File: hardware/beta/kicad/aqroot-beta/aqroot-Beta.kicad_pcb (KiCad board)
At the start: 4 copper layers, 74 x 155 mm, 188 parts, among them J1 CH280QV10-CT_50P, J2 Molex_5025700893, J3 USB_C_Receptacle_USB2.0_16P, J4 JST-PH-2 BATTERY, J5 COMMUNITY_HEADER_2x13, J6 JST-PH-2 SPEAKER, Q1 AO3400A, SW1 BOOT, SW2 UP, SW3 DOWN, SW4 LEFT, SW5 RIGHT, SW6 A_SELECT, SW7 B_BACK, SW8 HOME, SW9 SW_SPDT, U1 ESP32-S3-WROOM-1, U10 USBLC6-2SC6, U11 BQ25185, U12 TPS63020, U13 TPS61023, U14 MAX17048, U15 TPS22918, U16 TCA9517ADGK, U17 TPS61169DCKR, U2 TCA9535PWR, U3 TCA9535PWR, U4 BMI270, U5 MAX98357A, U6 TSOP38238, U7 E07-400M10S, U8 E22-900M22S, U9 ST25R3916-AQET

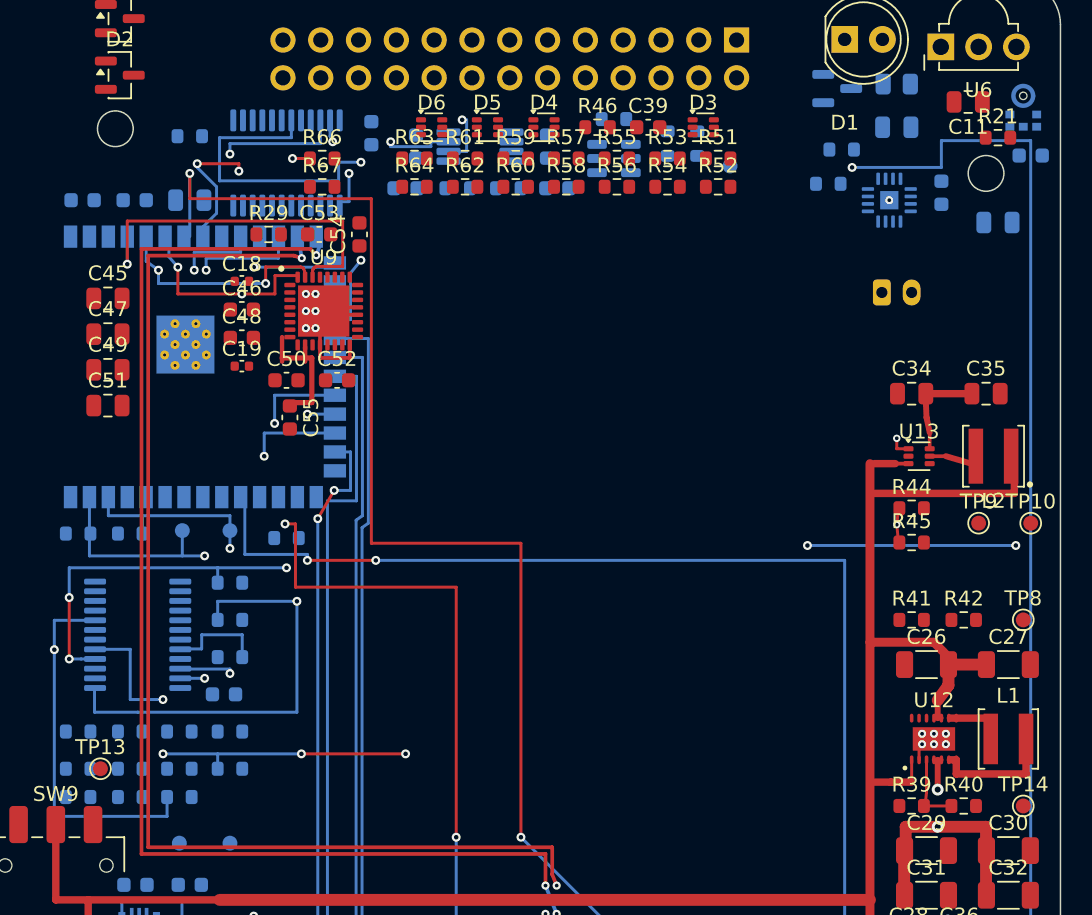
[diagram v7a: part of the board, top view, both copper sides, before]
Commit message: route +3V3 north backbone (Pass A: clusters F/C/B/A)
Builds the north +3V3 tree from the TPS63020 output island: 205.135 mm of
new copper in 57 tracks and 9 vias across B.Cu 38 / F.Cu 14 / In2 5. Board
ratsnest 405 -> 384, +3V3 ratsnest 69 -> 48, +3V3 islands 70 -> 49. DRC 0
electrical errors.

All 27 Pass-A pads now sit on ONE island with the U12 source: the six that
were already tied (U12.4, U12.5, C29.1, C30.1, C31.1, C32.1) plus the 21
routed here. Cluster F adds R39.1 and R41.1; cluster C adds U5.7, U5.8,
C9.1, C12.2, R24.2, C10.1, R21.1, C8.1, MK1.5, U15.1; cluster B adds
U16.1, C37.1, C40.1, C5.1, U3.24; cluster A adds C2.1, C3.1, R1.2, U1.2.

Topology is a single tree, not a star. The MCU spine runs first from the
U12 output at (65.400,54.250) west to U1.2, and every other load tees off
it with a short local branch - fifteen of the twenty branches are under
10 mm and eight are under 3 mm. The two long ones are structural rather
than star feeds: U5.8 at 30.481 mm reaches the north-east audio corner and
U15.1 at 24.873 mm crosses the 6.5 mm-tall corridor between HEADER
RESERVED (ends y 8.5) and NFC RESERVED (starts y 15), which is the only
legal west-east path at that latitude.

Widths: 0.600 mm everywhere except the In2 spine segment, widened to
0.800 mm, and one 0.500 mm single-pad branch into U5.7, whose pad admits no
0.600 mm centreline. Nothing drops below the 0.40 mm P3V3 outer-layer
minimum, so E6 is NOT used anywhere in this pass and no shared trunk is
necked. All nine vias are POWER-class 0.80/0.40.

The MCU spine measures 80.8 mohm end to end, dominated by its 27.700 mm
In2 run at 0.5 oz. That segment was opened from 0.600 to 0.800 mm - the
most the SX1262_RST_N In2 lane allows - taking the spine from 92.4 to
80.8 mohm. Drop is 8.1 mV at 100 mA browsing, 32.3 mV at the 400 mA WiFi TX
spike and 51.7 mV (1.57%) at the 640 mA heavy burst.

Three Pass-A pads are deferred with evidence rather than forced:

  U3.21  E6 CANNOT rescue it.  The pad is boxed b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
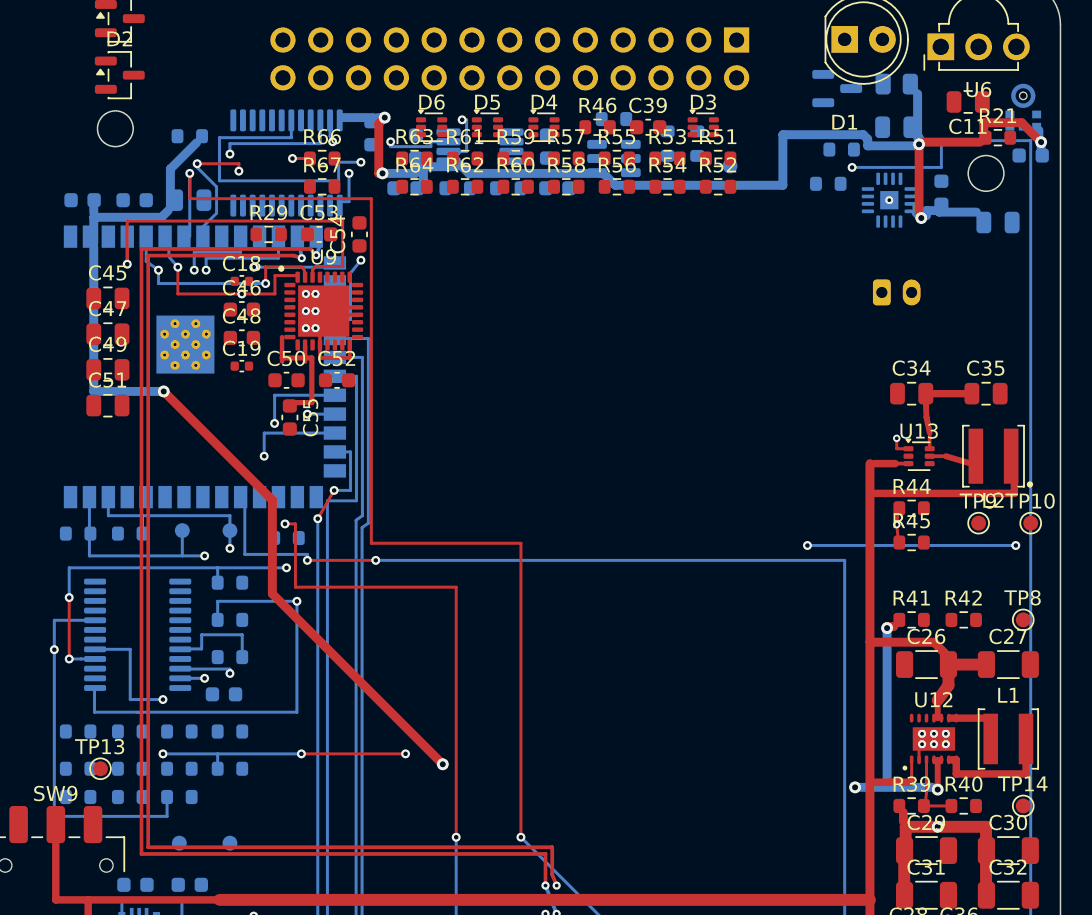
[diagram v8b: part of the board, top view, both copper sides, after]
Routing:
- net +3V3: track 76.0 -> 281.2 mm, vias 4 -> 13
